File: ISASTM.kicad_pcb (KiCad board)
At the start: 4 copper layers, 101.6 x 101.6 mm, 137 parts, among them J1 Bus_ISA_8bit, J2 USB_C_Receptacle_USB2.0, J3 Boot select, J4 USB_C_Receptacle_USB2.0, J5 TagConnect_TC2030_SWD, SW1 Reset, U1 STM32H743IITx, U10 SN74AVC8T245PW, U11 SN74AVC8T245PW, U12 SN74AVC8T245PW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

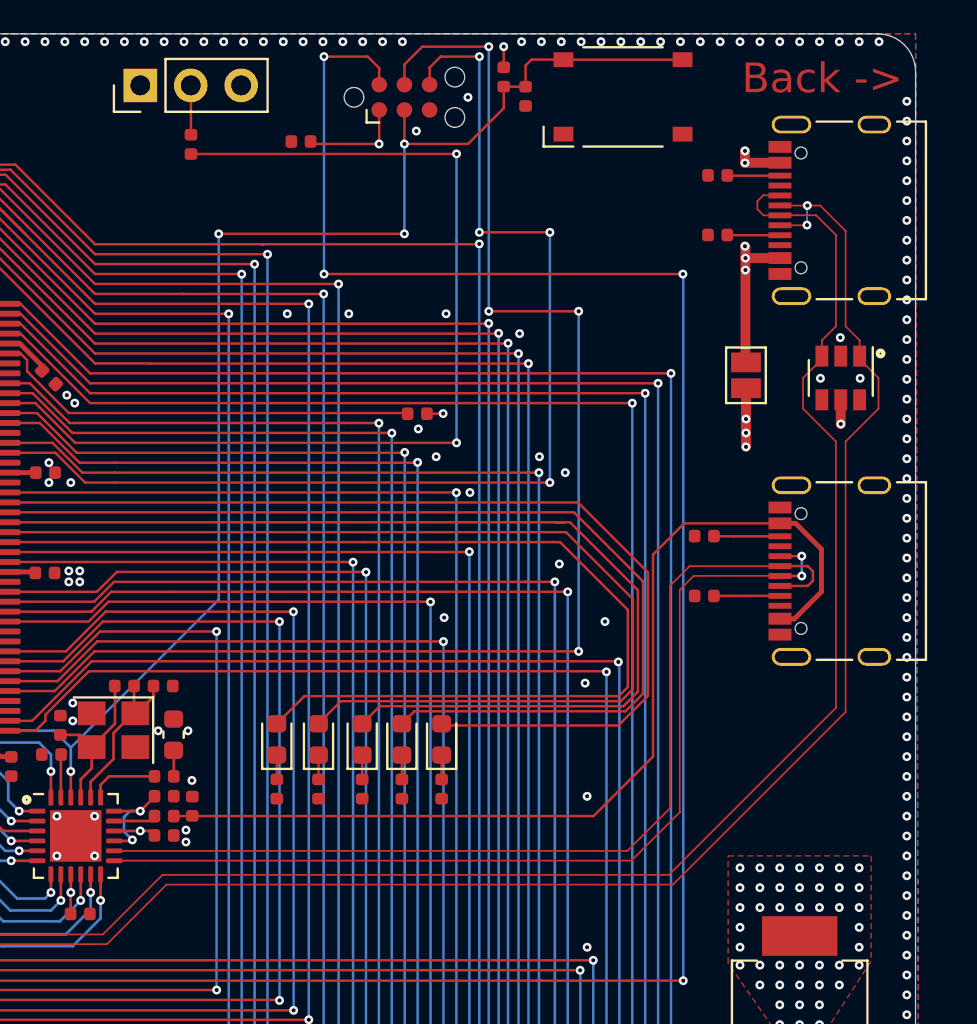
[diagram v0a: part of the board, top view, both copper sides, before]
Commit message: Add 3v3 testpoint
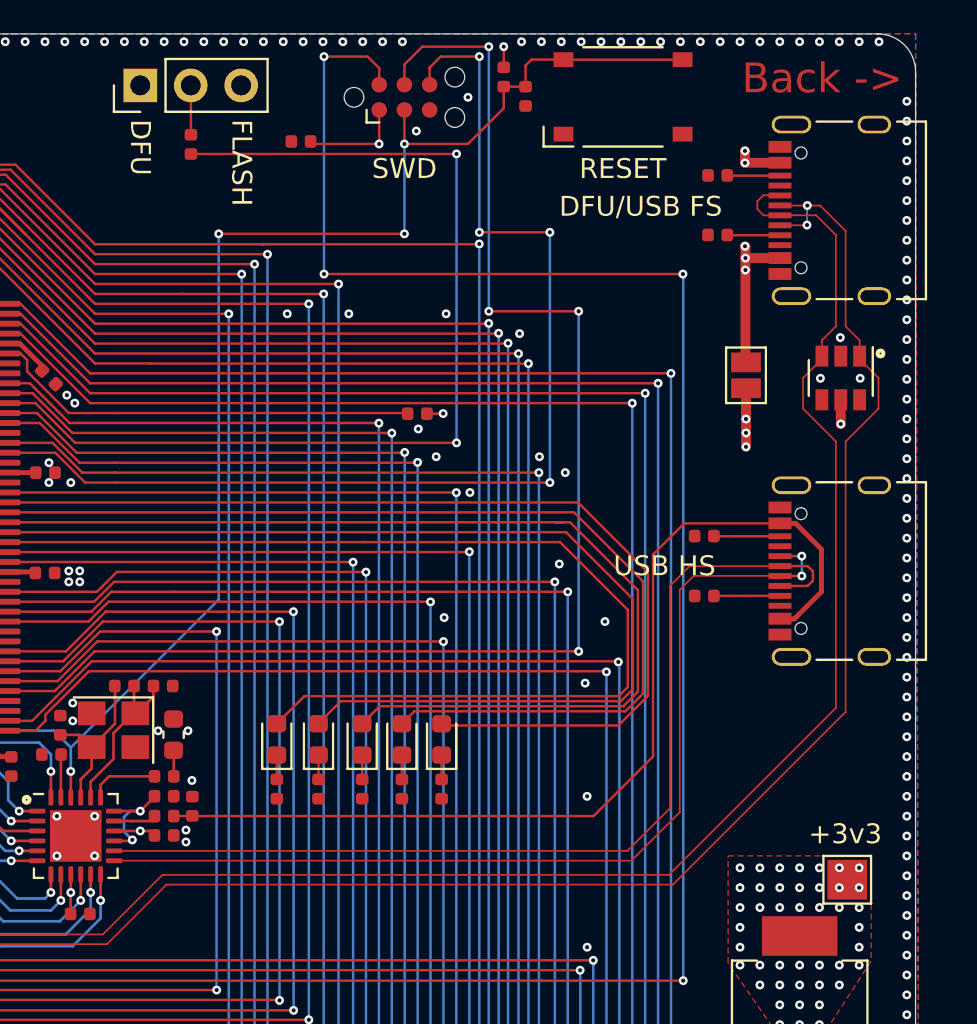
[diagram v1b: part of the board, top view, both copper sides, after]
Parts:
- added TP1: TestPoint, TestPoint:TestPoint_Pad_2.0x2.0mm, F.Cu at (113.4, 57.2)
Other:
- board text added: "+3v3"
- board text added: "DFU"
- board text added: "DFU/USB FS"
- board text added: "FLASH"
- board text added: "SWD"
- board text added: "USB HS"
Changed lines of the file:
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@@
   (general
     (thickness 1.6)
-    (drawings 98)
+    (drawings 105)
     (tracks 4971)
     (zones 0)
-    (modules 137)
+    (modules 138)
     (nets 267)
   )
@@
     (add_net "Net-(U8-Pad9)")
   )
+  (module TestPoint:TestPoint_Pad_2.0x2.0mm (layer F.Cu)
+    (at 113.4 57.2)
+    (descr "SMD rectangular pad as test Point, square 2.0mm side length")
+    (tags "test point SMD pad rectangle square")
+    (attr virtual)
+    (fp_text reference TP1 (at 0 -1.998) (layer F.SilkS) hide
+      (effects (font (size 1 1) (thickness 0.15)))
+    )
+    (fp_text value TestPoint (at 0 2.05) (layer F.Fab)
+      (effects (font (size 1 1) (thickness 0.15)))
+    )
+    (fp_text user %R (at 0 -2) (layer F.Fab)
+      (effects (font (size 1 1) (thickness 0.15)))
+    )
+    (fp_line (start -1.2 -1.2) (end 1.2 -1.2) (layer F.SilkS) (width 0.12))
+    (fp_line (start 1.2 -1.2) (end 1.2 1.2) (layer F.SilkS) (width 0.12))
+    (fp_line (start 1.2 1.2) (end -1.2 1.2) (layer F.SilkS) (width 0.12))
+    (fp_line (start -1.2 1.2) (end -1.2 -1.2) (layer F.SilkS) (width 0.12))
+    (fp_line (start -1.5 -1.5) (end 1.5 -1.5) (layer F.CrtYd) (width 0.05))
+    (fp_line (start -1.5 -1.5) (end -1.5 1.5) (layer F.CrtYd) (width 0.05))
+    (fp_line (start 1.5 1.5) (end 1.5 -1.5) (layer F.CrtYd) (width 0.05))
+    (fp_line (start 1.5 1.5) (end -1.5 1.5) (layer F.CrtYd) (width 0.05))
+    (pad 1 smd rect (at 0 0) (size 2 2) (layers F.Cu F.Mask)
+      (net 61 +3V3))
+  )
   (module Capacitor_SMD:C_0402_1005Metric (layer F.Cu)
     (at 106.2 89.383 90)
@@
       (net 32 GND))
   )
+  (gr_text +3v3 (at 113.3 54.9) (layer F.SilkS)
+    (effects (font (size 1 1) (thickness 0.15)))
+  )
+  (gr_text "USB HS" (at 104.2 41.4) (layer F.SilkS)
+    (effects (font (size 1 1) (thickness 0.15)))
+  )
+  (gr_text "DFU/USB FS" (at 103 23.3) (layer F.SilkS)
+    (effects (font (size 1 1) (thickness 0.15)))
+  )
+  (gr_text RESET (at 102.1 21.4) (layer F.SilkS)
+    (effects (font (size 1 1) (thickness 0.15)))
+  )
+  (gr_text SWD (at 91.1 21.4) (layer F.SilkS)
+    (effects (font (size 1 1) (thickness 0.15)))
+  )
+  (gr_text FLASH (at 82.9 18.9 270) (layer F.SilkS)
+    (effects (font (size 1 1) (thickness 0.15)) (justify left))
+  )
+  (gr_text DFU (at 77.8 18.9 270) (layer F.SilkS)
+    (effects (font (size 1 1) (thickness 0.15)) (justify left))
+  )
   (gr_text GND (at 114.3 107.32 90) (layer B.SilkS)

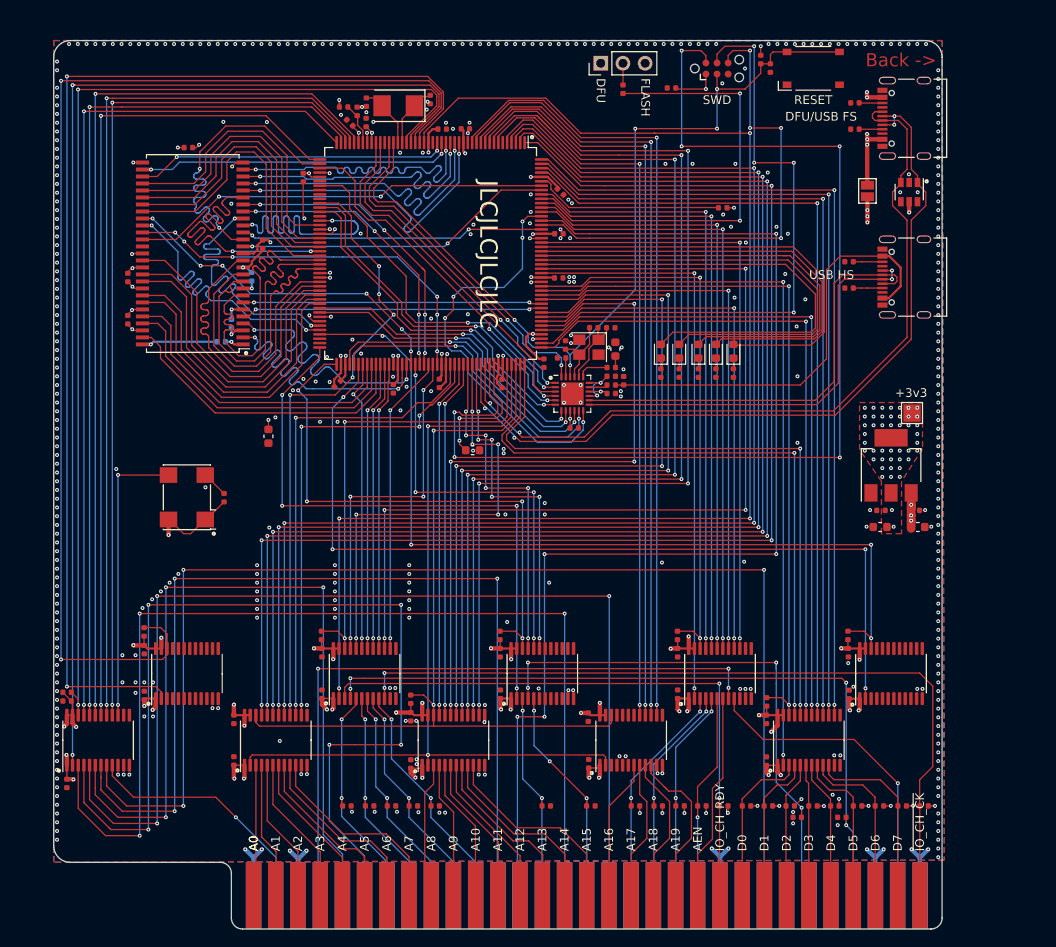
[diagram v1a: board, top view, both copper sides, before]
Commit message: Add tooling holes
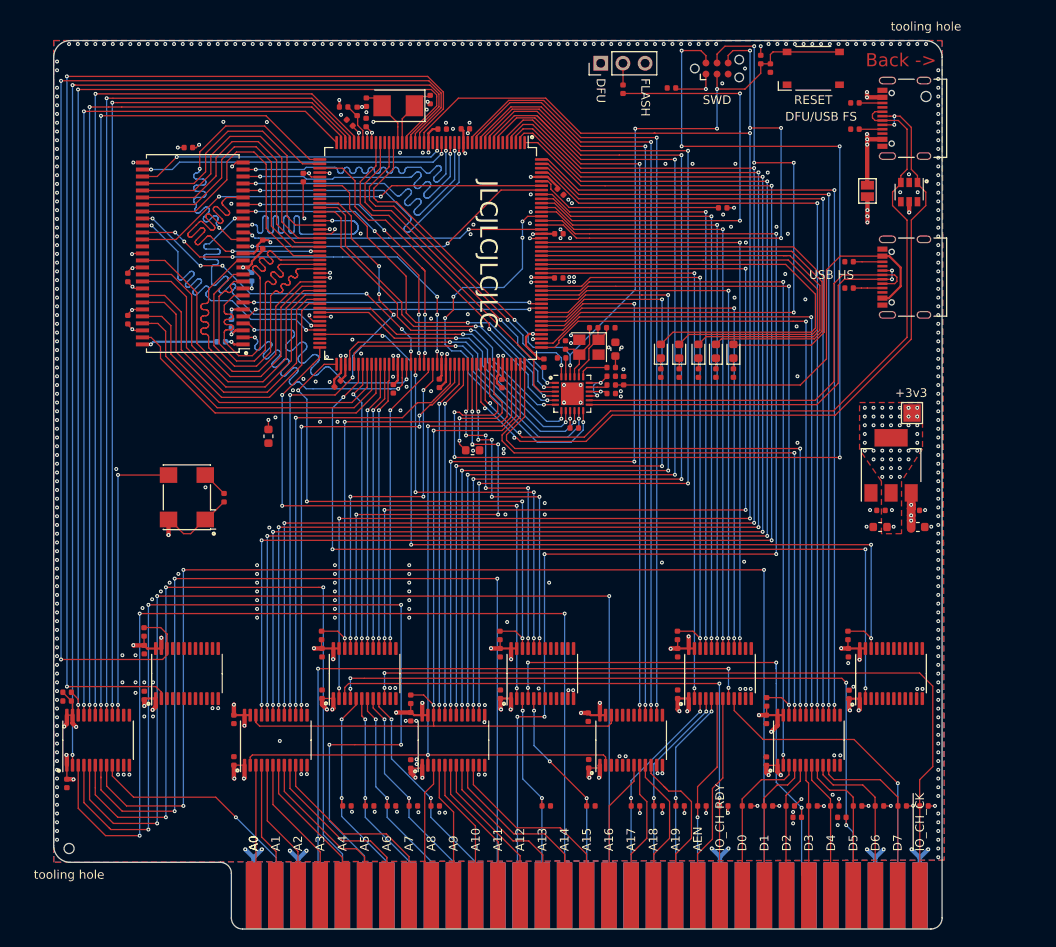
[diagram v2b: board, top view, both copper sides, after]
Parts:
- added H1: ToolingHole, ISASTM:ToolingHole_JLCSMT, F.Cu at (115.0, 21.0)
- added H2: ToolingHole, ISASTM:ToolingHole_JLCSMT, F.Cu at (17.0, 107.0)

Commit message: Match USB FS trace length
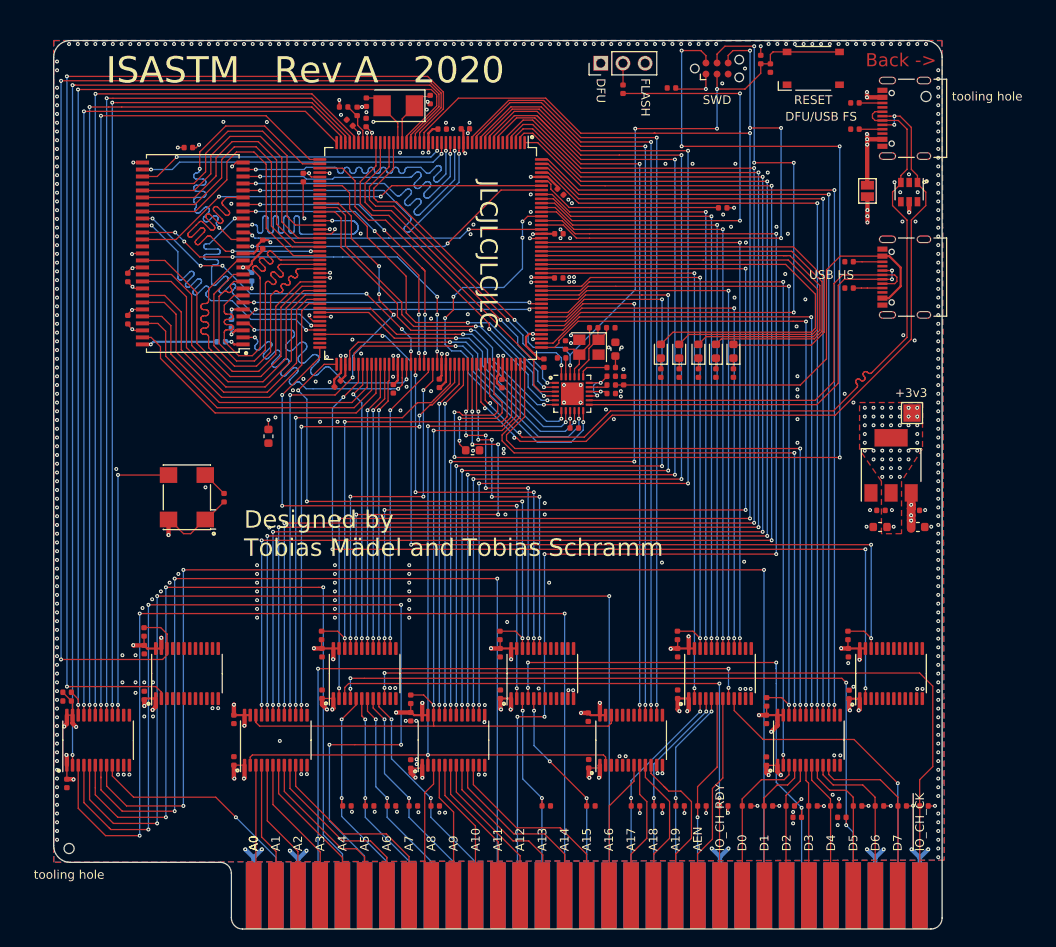
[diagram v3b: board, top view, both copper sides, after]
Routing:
- net /USB_FS_D+: track 90.6 -> 92.2 mm
- net GND: vias 473 -> 486
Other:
- board text added: "Designed by Tobias Mädel and Tobias Schramm"
- board text added: "ISASTM Rev A 2020"

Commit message: Prettier silkscreen markings, aesthetic fixes for traces
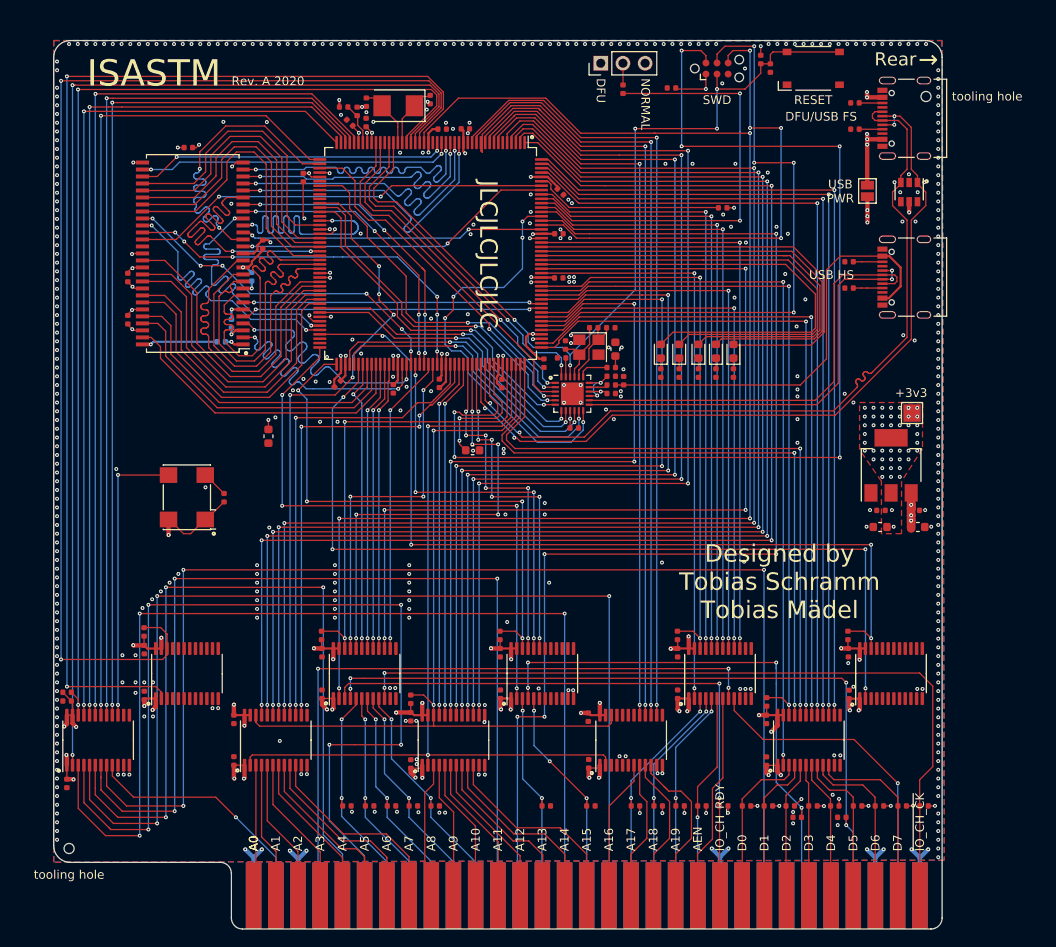
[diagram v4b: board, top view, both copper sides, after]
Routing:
- net /LV_A17: track 87.8 -> 90.2 mm
- net /LV_A13: track 113.9 -> 112.0 mm
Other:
- rule pad_to_mask_clearance: 0.05 -> 0
- board text added: "Designed by Tobias Schramm Tobias Mädel"
- board text added: "IRQ5"
- board text added: "IRQ7"
- board text added: "ISASTM"
- board text added: "NORMAL"
- board text added: "Rear"
- board text added: "Rev. A 2020"
- board text added: "USB PWR"
- board text added: "tbspace.de"
- board text added: "→"
- board text removed: "Back ->"
- board text removed: "Designed by Tobias Mädel and Tobias Schramm"
- board text removed: "FLASH"
- board text removed: "IRG5"
- board text removed: "IRG7"
- board text removed: "ISASTM Rev A 2020"
